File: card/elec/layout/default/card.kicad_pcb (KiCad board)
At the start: 2 copper layers, 99 x 55 mm, 3 parts

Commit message: [KICAD] add logo to front
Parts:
- added LED1: , lib:LED-SMD_L1.0-W0.5-RD, F.Cu at (160.0, 98.0)
- added R1: 62.5mW Thick Film Resistors 50V ±100ppm/℃ ±5% 50Ω 0402 Chip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, lib:R0402, F.Cu at (154.9, 98.0)
- C1: value 50V 50pF C0G ±5% 0402 Multilayer Ceramic Capacitors MLCC - SMD/SMT ROHS -> 16V 220nF X7R ±10% 0402 Multilayer Ceramic Capacitors MLCC - SMD/SMT ROHS
- moved U1 13.7 mm to (159.5, 93.5), turned to 180 degrees
- moved U2 8.44 mm to (152.4, 98.0), turned to 180 degrees
- moved C1 7.91 mm to (157.5, 98.0)
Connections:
- C1 pad 1: la -> vcc
- C1 pad 2: lb -> gnd
- U2 pad 7: vout -> vcc
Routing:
- net lb: track 1.70 -> 0.00 mm
- net la: track 1.68 -> 0.00 mm
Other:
- board size 99 x 55 mm -> 99.1 x 51 mm
- board text added: "Davide Asnaghi asnaghi@me.com"

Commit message: [KICAD] openvcf
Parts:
- moved U\ 40.6 mm to (192.8, 94.7), turned to 90 degrees
- moved R1 33.1 mm to (187.8, 94.7)
- moved C1 31.9 mm to (189.2, 94.8), turned to 90 degrees
- moved U1 31.1 mm to (190.6, 94.8), turned to 0 degrees
- moved LED1 30.8 mm to (190.6, 94.8), turned to -90 degrees
- renumbered U2 to U\
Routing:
- net gnd: track 0.00 -> 13.8 mm
- net lb: track 0.00 -> 11.0 mm, vias 0 -> 1
- net la: track 0.00 -> 9.35 mm, vias 0 -> 1
- net vcc: track 0.00 -> 5.64 mm
- net cathode: track 0.00 -> 3.61 mm
- added copper zone on B.Cu, net gnd
- added copper zone on F.Cu, net gnd
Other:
- board text added: "DAVIDE HW/SW ASNAGHI@ME.COM"
- board text removed: "Davide Asnaghi asnaghi@me.com"

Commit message: [KICAD] complete routing
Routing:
- net lb: track 11.0 -> 9.68 mm
- net la: track 9.35 -> 9.89 mm
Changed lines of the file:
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@@
     (at 190.627 94.75)
     (descr "<h1> Class 6 Antenna - 50 pF #01 </h1>\n<h3>\nSize: 	24 x 18 mm\n<br>\nWidth: 	0.25 mm\n<br>\nGap: 	0.1 mm\n<br>\nTurns: 	7\n</h3>")
-    (zone_connect 2)
     (attr through_hole)
     (fp_text reference "U1" (at 0 0) (layer "F.SilkS") hide
@@
     (fp_line (start 9.5 -7.95) (end 9.55 -7.95)
       (stroke (width 0.25) (type solid)) (layer "F.Cu"))
+    (fp_line (start 9.54 -1.116) (end 9.35 -0.94)
+      (stroke (width 0.25) (type default)) (layer "F.Cu"))
+    (fp_line (start 9.56 -4.25) (end 9.54 -1.116)
+      (stroke (width 0.25) (type solid)) (layer "F.Cu"))
     (fp_line (start 9.6 -8.3) (end 9.3 -8.3)
       (stroke (width 0.25) (type solid)) (layer "F.Cu"))
@@
     (fp_line (start 9.9 -6.6) (end 9.9 -5.55)
       (stroke (width 0.25) (type solid)) (layer "F.Cu"))
-    (fp_line (start 9.9 -5.55) (end 8.89 -5)
+    (fp_line (start 9.9 -5.55) (end 9.906 -4.826)
       (stroke (width 0.25) (type solid)) (layer "F.Cu"))
     (fp_line (start 9.9 -4.1) (end 9.9 6.45)
@@
     (fp_line (start 9.9 6.6) (end 9.9 6.45)
       (stroke (width 0.25) (type solid)) (layer "F.Cu"))
+    (fp_line (start 9.906 -4.826) (end 9.906 -4.572)
+      (stroke (width 0.25) (type solid)) (layer "F.Cu"))
+    (fp_line (start 9.906 -4.572) (end 9.56 -4.25)
+      (stroke (width 0.25) (type solid)) (layer "F.Cu"))
     (fp_line (start 10.25 -6.6) (end 10.25 -6.5)
       (stroke (width 0.25) (type solid)) (layer "F.Cu"))
@@
     (fp_line (start 12 -3.7) (end 12 -6.6)
       (stroke (width 0.25) (type solid)) (layer "F.Cu"))
-    (fp_line (start 12 6.6) (end 12 -2.5)
+    (fp_line (start 12 6.6) (end 12 0.635)
       (stroke (width 0.25) (type solid)) (layer "F.Cu"))
+    (fp_line (start 12.18 0.4) (end 12 0.635)
+      (stroke (width 0.25) (type default)) (layer "F.Cu"))
     (fp_arc (start -12 -6.6) (mid -11.297056 -8.297056) (end -9.6 -9)
       (stroke (width 0.25) (type solid)) (layer "F.Cu"))
@@
     (fp_arc (start 11.65 6.6) (mid 11.049569 8.049569) (end 9.6 8.65)
       (stroke (width 0.25) (type solid)) (layer "F.Cu"))
-    (fp_arc (start 12 -2.5) (mid 12.146447 -2.853553) (end 12.5 -3)
-      (stroke (width 0.25) (type solid)) (layer "F.Cu"))
     (fp_arc (start 12 6.6) (mid 11.297056 8.297056) (end 9.6 9)
       (stroke (width 0.25) (type solid)) (layer "F.Cu"))
-    (pad "1" thru_hole circle (at 8.89 -5) (size 0.7 0.7) (drill 0.3) (layers "*.Cu" "*.Mask")
-      (net 9 "la") (pintype "stereo") (clearance 0.2))
-    (pad "2" thru_hole circle (at 12.5 -3) (size 0.7 0.7) (drill 0.3) (layers "*.Cu" "*.Mask")
-      (net 2 "lb") (pintype "stereo") (clearance 0.2))
+    (pad "1" thru_hole circle (at 9.11 -0.82) (size 0.7 0.7) (drill 0.3) (layers "*.Cu" "*.Mask")
+      (net 9 "la") (pintype "stereo"))
+    (pad "2" thru_hole circle (at 12.33 0.18) (size 0.7 0.7) (drill 0.3) (layers "*.Cu" "*.Mask")
+      (net 2 "lb") (pintype "stereo"))
     (model "${KISYS3DMOD}/3D/misc_comp/NFC_Antenna_Class_6.step"
       (offset (xyz 0 0 0))
@@
     )
   )
-  (segment (start 193.421 94.72) (end 199.241 94.72) (width 0.25) (layer "F.Cu") (net 2))
-  (segment (start 199.241 94.72) (end 199.263 94.742) (width 0.25) (layer "F.Cu") (net 2))
-  (via (at 199.263 94.742) (size 0.8) (drill 0.4) (layers "F.Cu" "B.Cu") (net 2))
-  (segment (start 199.263 94.742) (end 202.255 91.75) (width 0.25) (layer "B.Cu") (net 2))
-  (segment (start 202.255 91.75) (end 203.127 91.75) (width 0.25) (layer "B.Cu") (net 2))
+  (segment (start 193.721 94.72) (end 193.421 94.72) (width 0.25) (layer "F.Cu") (net 2))
+  (segment (start 199.412996 94.996) (end 199.354996 94.938) (width 0.25) (layer "F.Cu") (net 2))
+  (segment (start 199.354996 94.938) (end 193.939 94.938) (width 0.25) (layer "F.Cu") (net 2))
+  (segment (start 199.802 94.996) (end 199.412996 94.996) (width 0.25) (layer "F.Cu") (net 2))
+  (segment (start 193.939 94.938) (end 193.721 94.72) (width 0.25) (layer "F.Cu") (net 2))
+  (via (at 199.802 94.996) (size 0.8) (drill 0.4) (layers "F.Cu" "B.Cu") (net 2))
+  (segment (start 202.957 94.93) (end 199.868 94.93) (width 0.25) (layer "B.Cu") (net 2))
+  (segment (start 199.868 94.93) (end 199.802 94.996) (width 0.25) (layer "B.Cu") (net 2))
   (segment (start 188.341 93.472) (end 189.865 93.472) (width 0.25) (layer "F.Cu") (net 3))
   (segment (start 187.833 94.22) (end 187.833 93.98) (width 0.25) (layer "F.Cu") (net 3))
@@
   (segment (start 186.182 93.218) (end 186.182 94.996) (width 0.25) (layer "F.Cu") (net 8))
   (segment (start 192.821 92.999) (end 192.024 92.202) (width 0.25) (layer "F.Cu") (net 8))
-  (segment (start 193.321 94.07) (end 197.522 94.07) (width 0.25) (layer "F.Cu") (net 9))
-  (segment (start 197.522 94.07) (end 199.517 92.075) (width 0.25) (layer "F.Cu") (net 9))
-  (via (at 199.517 92.075) (size 0.8) (drill 0.4) (layers "F.Cu" "B.Cu") (net 9))
-  (segment (start 199.517 92.075) (end 199.517 89.75) (width 0.25) (layer "B.Cu") (net 9))
+  (segment (start 199.1686 94.488) (end 199.595863 94.060737) (width 0.25) (layer "F.Cu") (net 9))
+  (segment (start 193.321 94.07) (end 193.796 94.07) (width 0.25) (layer "F.Cu") (net 9))
+  (segment (start 194.214 94.488) (end 199.1686 94.488) (width 0.25) (layer "F.Cu") (net 9))
+  (segment (start 193.796 94.07) (end 194.214 94.488) (width 0.25) (layer "F.Cu") (net 9))
+  (via (at 203.002 93.93) (size 0.8) (drill 0.4) (layers "F.Cu" "B.Cu") (net 9))
+  (segment (start 203.002 93.93) (end 199.737 93.93) (width 0.25) (layer "B.Cu") (net 9))
   (zone (net 8) (net_name "gnd") (layers "F&B.Cu") (hatch edge 0.5)
     (connect_pads (clearance 0.5))

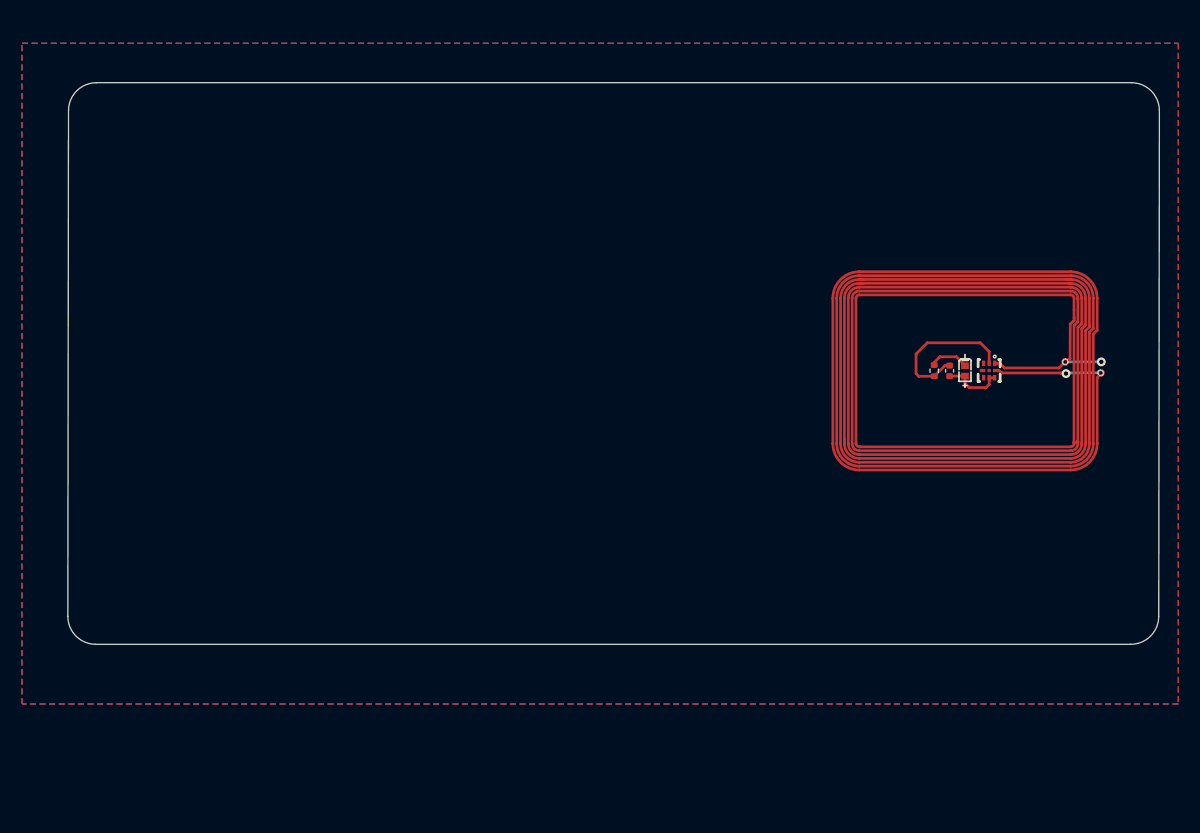
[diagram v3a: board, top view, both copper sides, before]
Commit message: [KICAD] remove copper from under the antenna
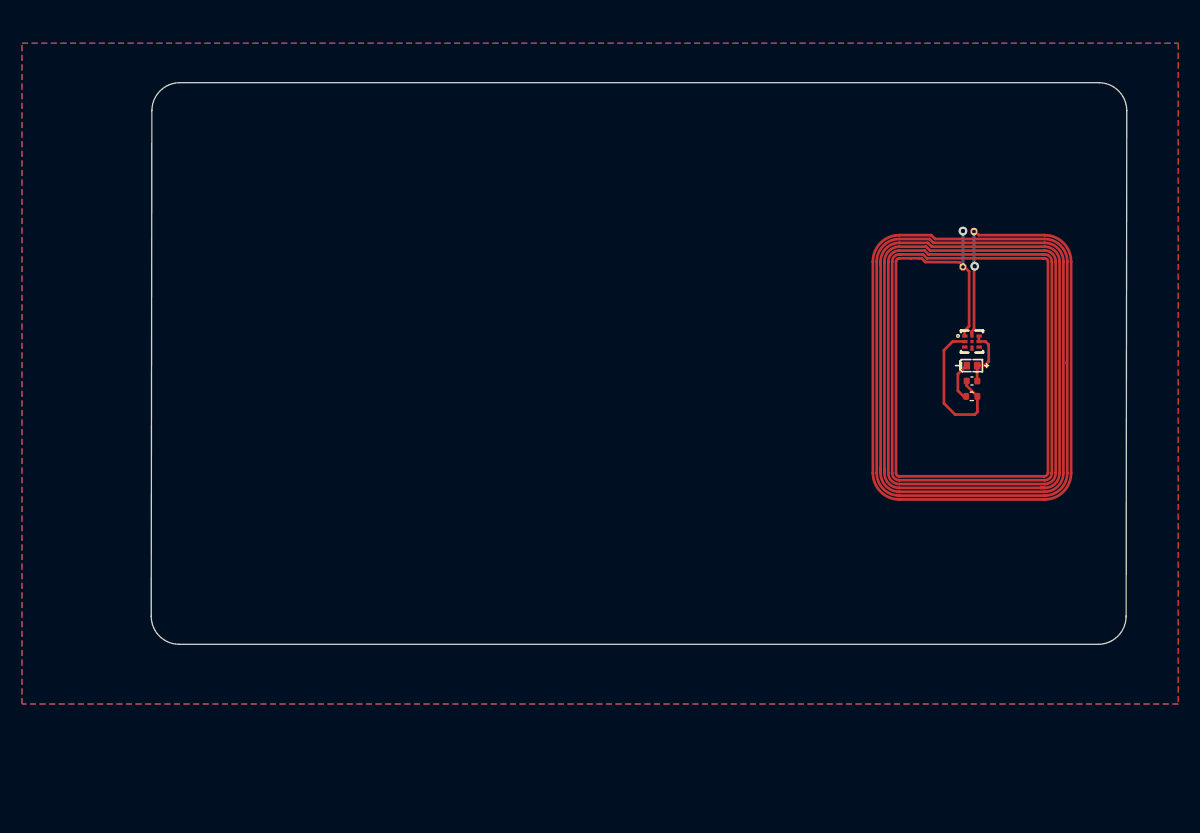
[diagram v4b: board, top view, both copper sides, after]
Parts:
- removed U\: , lib:XQFN-8_L1.6-W1.6-P0.50-BR
- added U2: , lib:XQFN-8_L1.6-W1.6-P0.50-BR, F.Cu at (191.3, 92.1)
- moved R1 4.13 mm to (191.2, 97.1), turned to 0 degrees
- moved C1 2.23 mm to (191.3, 95.7), turned to 180 degrees
- moved LED1 0.79 mm to (191.3, 94.3), turned to 0 degrees
- moved U1 0.71 mm to (191.3, 94.4), turned to 90 degrees
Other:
- board size 99.1 x 51 mm -> 88.6 x 51 mm

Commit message: [OPENVCF] remove copper from antenna
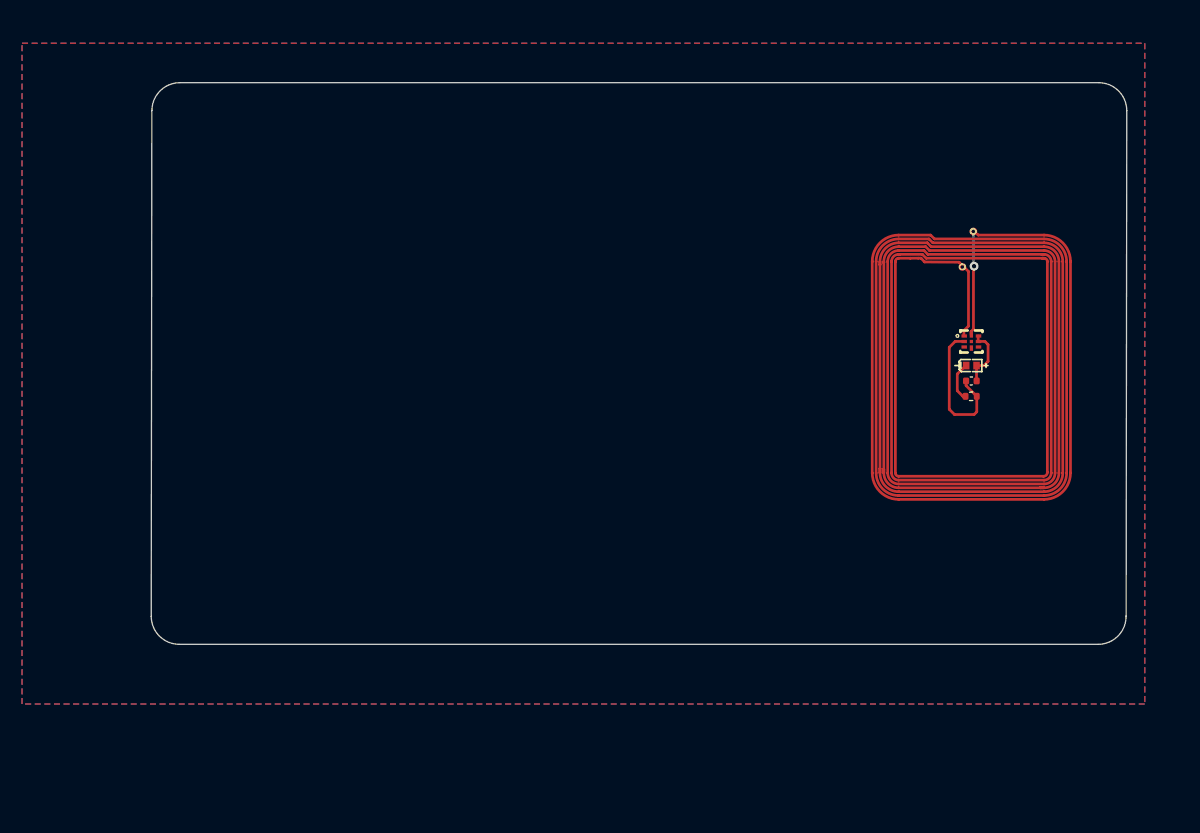
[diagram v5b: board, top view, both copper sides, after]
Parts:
- moved C1 0.06 mm to (191.2, 95.7)
- moved LED1 0.06 mm to (191.2, 94.3)
- moved U1 0.06 mm to (191.2, 94.4)
- moved U2 0.06 mm to (191.2, 92.1)
- moved R1 0.06 mm to (191.2, 97.1)
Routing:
- net la: track 9.89 -> 6.62 mm, vias 1 -> 0
- net gnd: track 13.8 -> 13.2 mm
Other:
- board text added: "SCHEMATX HW/SW"
- board text removed: "DAVIDE HW/SW ASNAGHI@ME.COM"

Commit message: [LOGO] use dxf
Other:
- board text added: "DIODE INC. HW/SW"
- board text removed: "SCHEMATX HW/SW"

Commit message: [ATOPILE] logo
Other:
- board text added: "atopile.io"
- board text removed: "DIODE INC. HW/SW"
